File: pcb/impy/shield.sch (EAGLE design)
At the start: 117 parts, among them J1 USB-2410-06, J2 SI-60062-F, J3 5V, U1 AD5933YRS, U10 LTC3406AB, U11 23LCV1024-I/SN, U12 MIC2009A-1YM6, U13 ADG725BSU, U14 ADG725BSU, U2 ADG704BRM, U3 AD8656ARZ, U4 M24C08WMN, U5 ADG706BRU, U6 DP83848I, U7 MIC2009A-1YM6, U8 AT25DF081A-SS, U9 SST25VF080B-80-4I-S2

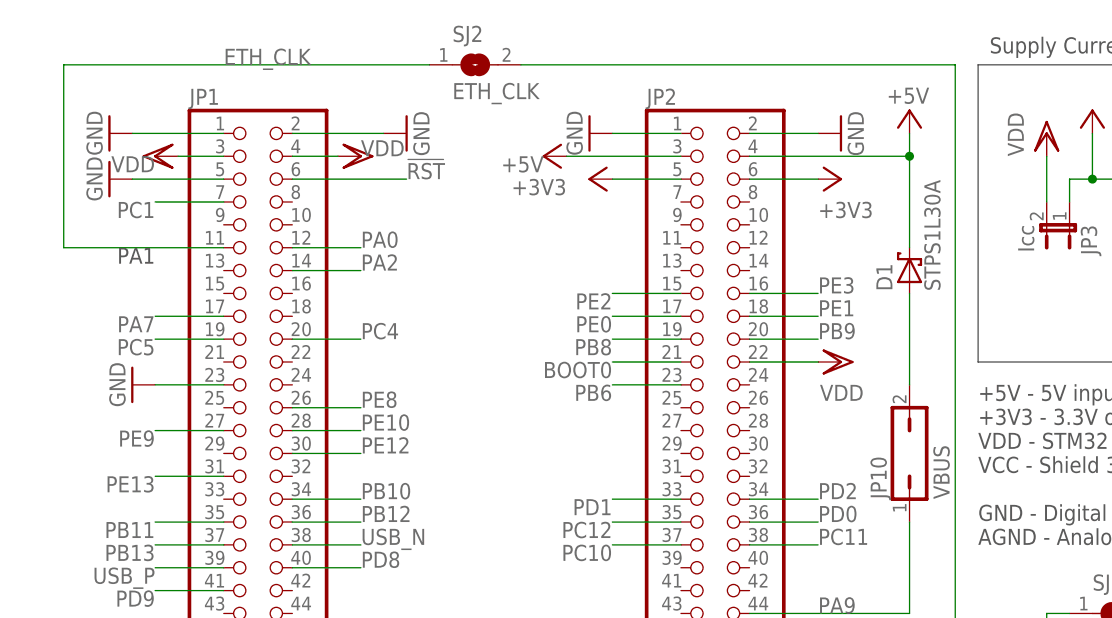
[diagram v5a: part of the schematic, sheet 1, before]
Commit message: * pcb/impy: (shield.sch, shield.brd) Change feedback mux selection signals (PE8, PE9, PE10 to PB4, PB5, PB7) and layout.
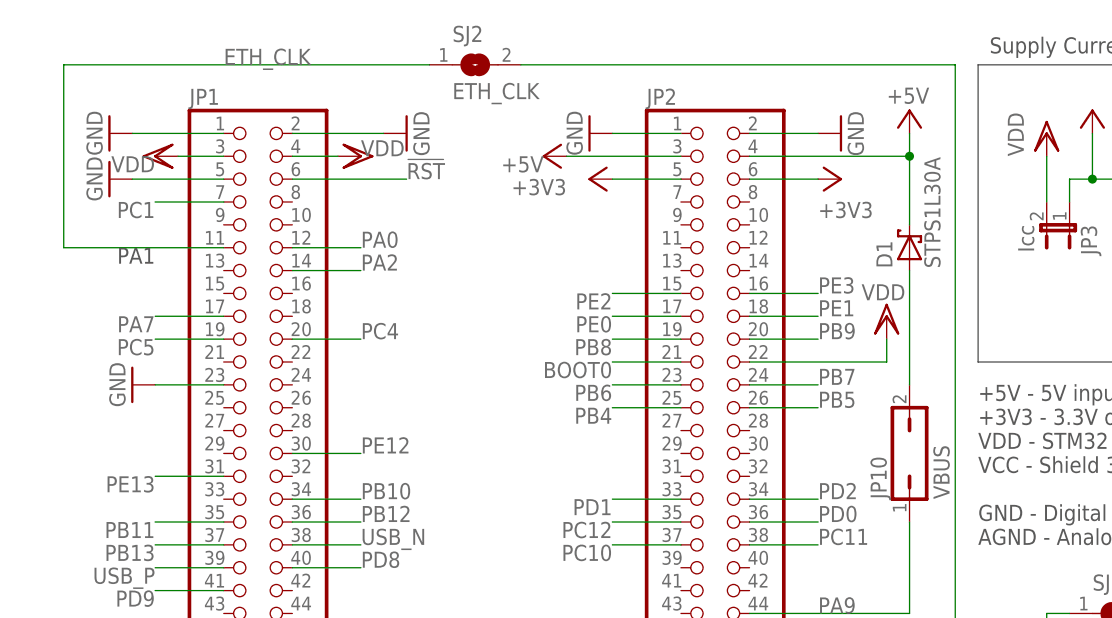
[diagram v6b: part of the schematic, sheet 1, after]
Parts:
- removed R20: 10k, rcl:R-EU_R0603
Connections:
- removed net N$107: R20.1, U5.EN
- removed net PE10: JP1.28, U5.A2
- removed net PE8: JP1.26, U5.A0
- removed net PE9: JP1.27, U5.A1
- new net PB4: JP2.25, U5.A1
- new net PB5: JP2.26, U5.A2
- new net PB7: JP2.24, U5.A0
- net VCC: now also U5.EN; no longer R20.2
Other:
- moved on the sheet: D1
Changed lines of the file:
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@@
 <attribute name="TP_SIGNAL_NAME" value="MAC_CLK"/>
 </part>
-<part name="R20" library="rcl" deviceset="R-EU_" device="R0603" value="10k"/>
 <part name="GND44" library="supply1" deviceset="GND" device=""/>
 <part name="P+36" library="supply1" deviceset="+5V" device=""/>
@@
 <attribute name="VALUE" x="12.7" y="78.74" size="1.778" layer="96" rot="R180"/>
 </instance>
-<instance part="VDD3" gate="G$1" x="88.9" y="55.88" smashed="yes" rot="R270">
-<attribute name="VALUE" x="91.44" y="53.34" size="1.778" layer="96" rot="R180"/>
+<instance part="VDD3" gate="G$1" x="93.98" y="60.96" smashed="yes">
+<attribute name="VALUE" x="91.186" y="62.738" size="1.778" layer="96"/>
 </instance>
 <instance part="GND9" gate="1" x="60.96" y="81.28" rot="R270"/>
@@
 <instance part="U12" gate="G$1" x="142.24" y="76.2"/>
 <instance part="GND35" gate="1" x="127" y="76.2" rot="R270"/>
-<instance part="D1" gate="G$1" x="96.52" y="66.04" rot="R90"/>
+<instance part="D1" gate="G$1" x="96.52" y="68.58" rot="R90"/>
 <instance part="R12" gate="G$1" x="154.94" y="68.58" smashed="yes" rot="R90">
 <attribute name="NAME" x="153.4414" y="64.77" size="1.778" layer="95" rot="R90"/>
@@
 <pinref part="VDD3" gate="G$1" pin="VDD"/>
 <pinref part="JP2" gate="A" pin="22"/>
-<wire x1="86.36" y1="55.88" x2="78.74" y2="55.88" width="0.1524" layer="91"/>
+<wire x1="93.98" y1="58.42" x2="93.98" y2="55.88" width="0.1524" layer="91"/>
+<wire x1="93.98" y1="55.88" x2="78.74" y2="55.88" width="0.1524" layer="91"/>
 </segment>
 <segment>
@@
 <wire x1="96.52" y1="78.74" x2="96.52" y2="81.28" width="0.1524" layer="91"/>
 <pinref part="D1" gate="G$1" pin="C"/>
-<wire x1="96.52" y1="68.58" x2="96.52" y2="78.74" width="0.1524" layer="91"/>
+<wire x1="96.52" y1="71.12" x2="96.52" y2="78.74" width="0.1524" layer="91"/>
 <junction x="96.52" y="78.74"/>
 </segment>
@@
 <wire x1="71.12" y1="40.64" x2="63.5" y2="40.64" width="0.1524" layer="91"/>
 <label x="63.5" y="40.64" size="1.778" layer="95" rot="R180"/>
-</segment>
-</net>
-<net name="PE8" class="0">
-<segment>
-<pinref part="JP1" gate="A" pin="26"/>
-<wire x1="27.94" y1="50.8" x2="35.56" y2="50.8" width="0.1524" layer="91"/>
-<label x="35.56" y="50.8" size="1.778" layer="95"/>
-</segment>
-</net>
-<net name="PE10" class="0">
-<segment>
-<pinref part="JP1" gate="A" pin="28"/>
-<wire x1="27.94" y1="48.26" x2="35.56" y2="48.26" width="0.1524" layer="91"/>
-<label x="35.56" y="48.26" size="1.778" layer="95"/>
-</segment>
-</net>
-<net name="PE9" class="0">
-<segment>
-<pinref part="JP1" gate="A" pin="27"/>
-<wire x1="20.32" y1="48.26" x2="12.7" y2="48.26" width="0.1524" layer="91"/>
-<label x="12.7" y="48.26" size="1.778" layer="95" rot="R180"/>
 </segment>
 </net>
@@
 <pinref part="JP10" gate="A" pin="2"/>
 <pinref part="D1" gate="G$1" pin="A"/>
-<wire x1="96.52" y1="53.34" x2="96.52" y2="63.5" width="0.1524" layer="91"/>
+<wire x1="96.52" y1="53.34" x2="96.52" y2="66.04" width="0.1524" layer="91"/>
 </segment>
 </net>
@@
 <wire x1="152.4" y1="81.28" x2="160.02" y2="81.28" width="0.1524" layer="91"/>
 <wire x1="160.02" y1="81.28" x2="160.02" y2="78.74" width="0.1524" layer="91"/>
+</segment>
+</net>
+<net name="PB7" class="0">
+<segment>
+<pinref part="JP2" gate="A" pin="24"/>
+<wire x1="78.74" y1="53.34" x2="86.36" y2="53.34" width="0.1524" layer="91"/>
+<label x="86.36" y="53.34" size="1.778" layer="95"/>
+</segment>
+</net>
+<net name="PB5" class="0">
+<segment>
+<pinref part="JP2" gate="A" pin="26"/>
+<wire x1="78.74" y1="50.8" x2="86.36" y2="50.8" width="0.1524" layer="91"/>
+<label x="86.36" y="50.8" size="1.778" layer="95"/>
+</segment>
+</net>
+<net name="PB4" class="0">
+<segment>
+<pinref part="JP2" gate="A" pin="25"/>
+<wire x1="71.12" y1="50.8" x2="63.5" y2="50.8" width="0.1524" layer="91"/>
+<label x="63.5" y="50.8" size="1.778" layer="95" rot="R180"/>
 </segment>
 </net>
@@
 <instance part="U5" gate="G$1" x="127" y="83.82"/>
 <instance part="P+32" gate="VCC" x="144.78" y="66.04" rot="R270"/>
-<instance part="P+33" gate="VCC" x="157.48" y="63.5" rot="MR0"/>
+<instance part="P+33" gate="VCC" x="144.78" y="58.42" rot="MR90"/>
 <instance part="AGND7" gate="VR1" x="149.86" y="63.5" rot="MR270"/>
 <instance part="RFB1" gate="G$1" x="91.44" y="109.22" smashed="yes" rot="R180">
@@
 <instance part="TP11" gate="G$1" x="35.56" y="88.9"/>
 <instance part="AGND14" gate="VR1" x="35.56" y="81.28" rot="MR0"/>
-<instance part="R20" gate="G$1" x="147.32" y="58.42"/>
 <instance part="AGND15" gate="VR1" x="111.76" y="53.34" smashed="yes">
 <attribute name="VALUE" x="111.76" y="55.88" size="1.778" layer="96" rot="R180"/>
@@
 </segment>
 <segment>
-<pinref part="R20" gate="G$1" pin="2"/>
+<pinref part="U5" gate="G$1" pin="EN"/>
+<wire x1="142.24" y1="58.42" x2="139.7" y2="58.42" width="0.1524" layer="91"/>
 <pinref part="P+33" gate="VCC" pin="VCC"/>
-<wire x1="152.4" y1="58.42" x2="157.48" y2="58.42" width="0.1524" layer="91"/>
-<wire x1="157.48" y1="58.42" x2="157.48" y2="60.96" width="0.1524" layer="91"/>
 </segment>
 </net>
@@
 </segment>
 </net>
-<net name="PE8" class="0">
+<net name="PB7" class="0">
 <segment>
 <pinref part="U5" gate="G$1" pin="A0"/>
@@
 </segment>
 </net>
-<net name="PE9" class="0">
+<net name="PB4" class="0">
 <segment>
 <pinref part="U5" gate="G$1" pin="A1"/>
@@
 </segment>
 </net>
-<net name="PE10" class="0">
+<net name="PB5" class="0">
 <segment>
 <pinref part="U5" gate="G$1" pin="A2"/>
@@
 </segment>
 </net>
-<net name="N$107" class="0">
-<segment>
-<pinref part="R20" gate="G$1" pin="1"/>
-<pinref part="U5" gate="G$1" pin="EN"/>
-<wire x1="142.24" y1="58.42" x2="139.7" y2="58.42" width="0.1524" layer="91"/>
-</segment>
-</net>

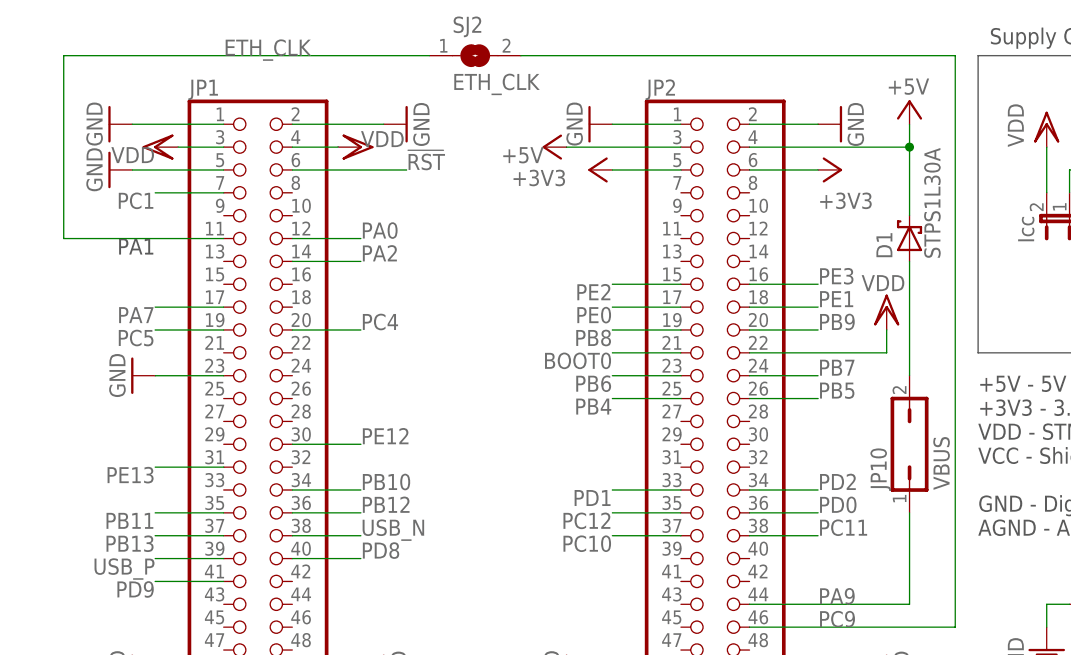
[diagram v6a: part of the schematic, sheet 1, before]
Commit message: * pcb/impy: (shield.sch) Change attenuation mux signals (PE12, PE13 to PE5, PE6).   (shield.brd) Layout new attenuation mux signals. Optimize layout of +5V and I2C.
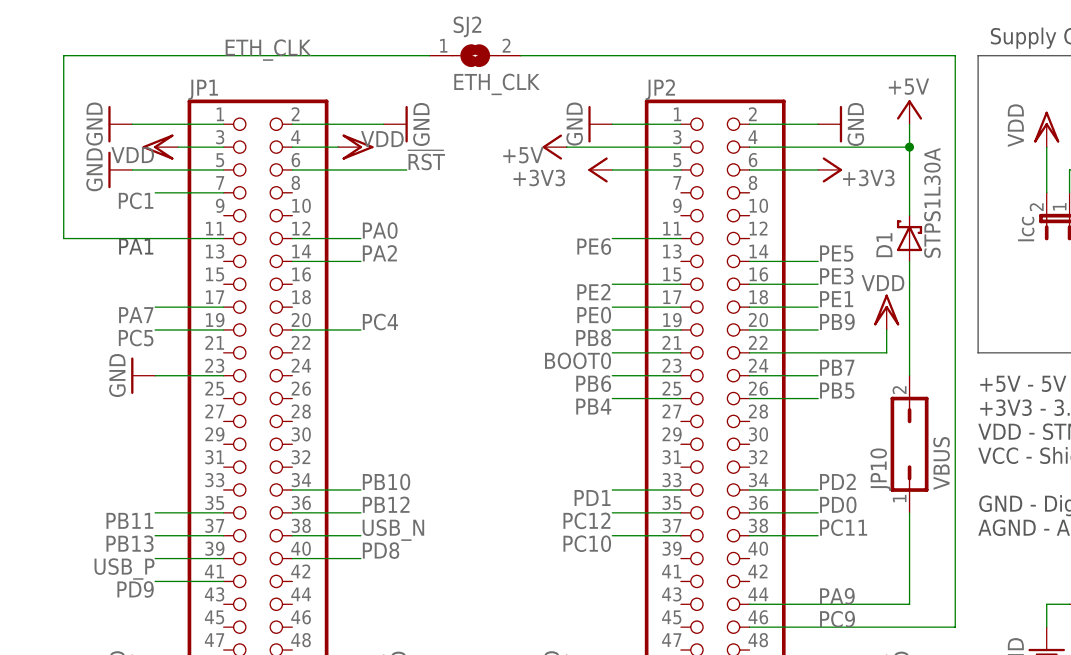
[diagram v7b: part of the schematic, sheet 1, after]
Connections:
- removed net PE12: JP1.30, U2.A0
- removed net PE13: JP1.31, U2.A1
- new net PE5: JP2.14, U2.A0
- new net PE6: JP2.11, U2.A1
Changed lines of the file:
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@@
 </instance>
 <instance part="+3V1" gate="G$1" x="88.9" y="76.2" smashed="yes" rot="MR90">
-<attribute name="VALUE" x="86.36" y="73.66" size="1.778" layer="96" rot="MR180"/>
+<attribute name="VALUE" x="88.9" y="76.2" size="1.778" layer="96" rot="MR180"/>
 </instance>
 <instance part="+3V2" gate="G$1" x="60.96" y="76.2" smashed="yes" rot="R90">
@@
 <wire x1="71.12" y1="40.64" x2="63.5" y2="40.64" width="0.1524" layer="91"/>
 <label x="63.5" y="40.64" size="1.778" layer="95" rot="R180"/>
-</segment>
-</net>
-<net name="PE12" class="0">
-<segment>
-<pinref part="JP1" gate="A" pin="30"/>
-<wire x1="27.94" y1="45.72" x2="35.56" y2="45.72" width="0.1524" layer="91"/>
-<label x="35.56" y="45.72" size="1.778" layer="95"/>
-</segment>
-</net>
-<net name="PE13" class="0">
-<segment>
-<pinref part="JP1" gate="A" pin="31"/>
-<wire x1="12.7" y1="43.18" x2="20.32" y2="43.18" width="0.1524" layer="91"/>
-<label x="12.7" y="43.18" size="1.778" layer="95" rot="R180"/>
 </segment>
 </net>
@@
 </segment>
 </net>
+<net name="PE5" class="0">
+<segment>
+<pinref part="JP2" gate="A" pin="14"/>
+<wire x1="78.74" y1="66.04" x2="86.36" y2="66.04" width="0.1524" layer="91"/>
+<label x="86.36" y="66.04" size="1.778" layer="95"/>
+</segment>
+</net>
+<net name="PE6" class="0">
+<segment>
+<pinref part="JP2" gate="A" pin="11"/>
+<wire x1="71.12" y1="68.58" x2="63.5" y2="68.58" width="0.1524" layer="91"/>
+<label x="63.5" y="68.58" size="1.778" layer="95" rot="R180"/>
+</segment>
+</net>
 </nets>
 </sheet>
@@
 </segment>
 </net>
-<net name="PE13" class="0">
+<net name="PE6" class="0">
 <segment>
 <pinref part="U2" gate="G$1" pin="A1"/>
@@
 </segment>
 </net>
-<net name="PE12" class="0">
+<net name="PE5" class="0">
 <segment>
 <pinref part="U2" gate="G$1" pin="A0"/>

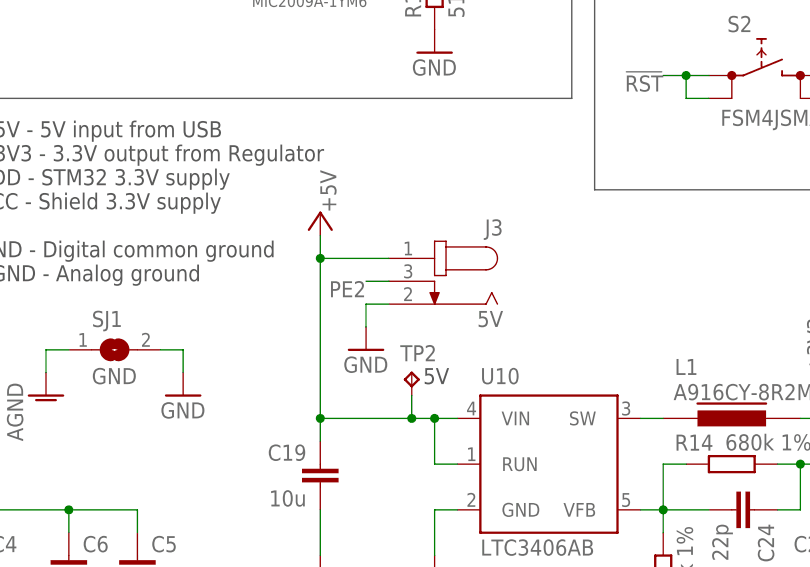
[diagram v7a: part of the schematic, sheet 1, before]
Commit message: * pcb/impy: (shield.sch, shield.brd) Replace surface mount DC power jack by through hole version.
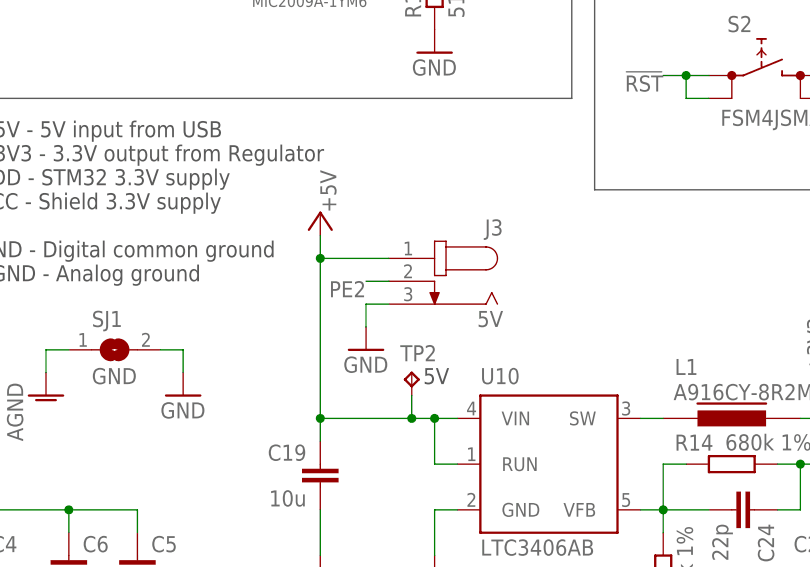
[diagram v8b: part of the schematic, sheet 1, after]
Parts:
- J3: device parts:JACK-PLUG-S2.5 -> parts:JACK-PLUG-T2.5
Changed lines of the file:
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@@
 <part name="GND38" library="supply1" deviceset="GND" device=""/>
 <part name="JP10" library="jumper" deviceset="JP1Q" device="" value="VBUS"/>
-<part name="J3" library="parts" deviceset="JACK-PLUG" device="-S2.5" value="5V"/>
+<part name="J3" library="parts" deviceset="JACK-PLUG" device="-T2.5" value="5V"/>
 <part name="GND39" library="supply1" deviceset="GND" device=""/>
 <part name="U12" library="parts" deviceset="MIC2009A-1" device="YM6"/>
